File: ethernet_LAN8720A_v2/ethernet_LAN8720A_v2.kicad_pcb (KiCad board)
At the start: 2 copper layers, 55.2 x 65.4 mm, 47 parts, among them P1 SI-52003-F, P3 PoE, U1 LAN8720A-CP, U2 ASV-50.000MHZ-E-T

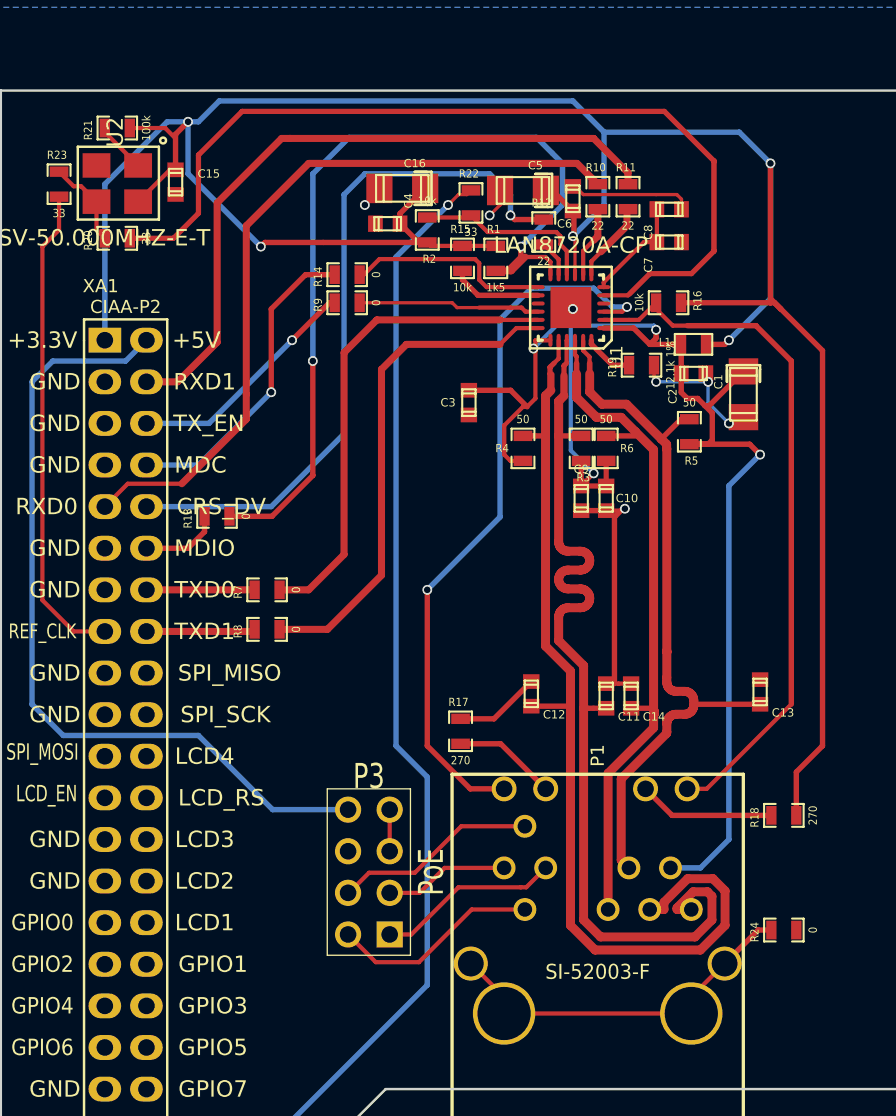
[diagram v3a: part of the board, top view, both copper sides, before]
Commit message: Acomdado de serigrafía y algunas pistas para que el pleno llegue a toda la placa.
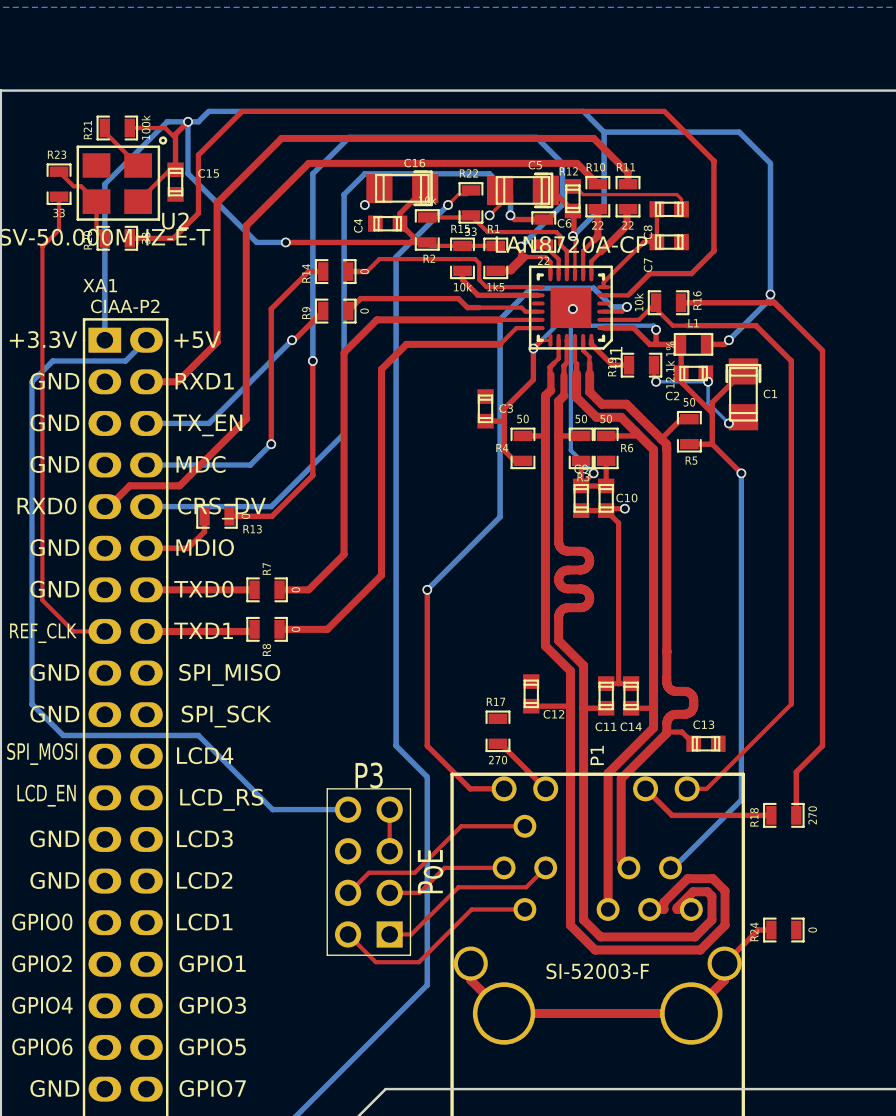
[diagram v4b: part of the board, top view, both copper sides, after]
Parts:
- moved C13 4.57 mm to (134.2, 108.6), turned to 180 degrees
- moved R17 2.29 mm to (121.5, 107.9)
- moved C3 1.09 mm to (120.8, 88.2), turned to 270 degrees
- moved R9 0.86 mm to (111.6, 82.2)
- moved R14 0.72 mm to (111.6, 79.8)
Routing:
- net +3.3V: track 171.0 -> 162.0 mm
- net Net-(C1-Pad1): track 89.0 -> 80.9 mm
- net GND: track 43.5 -> 39.9 mm
- net Net-(P1-Pad13): track 6.34 -> 4.05 mm
- net /Circuito Principal/Rx_P: track 45.1 -> 43.0 mm
- net Net-(P1-Pad16): track 22.9 -> 24.9 mm
- net /Circuito Principal/MDC: track 19.3 -> 20.5 mm
- net Net-(R9-Pad2): track 11.1 -> 12.2 mm
- net /Circuito Principal/TXEN: track 14.5 -> 13.6 mm
- net Net-(R14-Pad2): track 12.6 -> 13.2 mm
- net /Circuito Principal/Tx_P: track 59.0 -> 58.5 mm

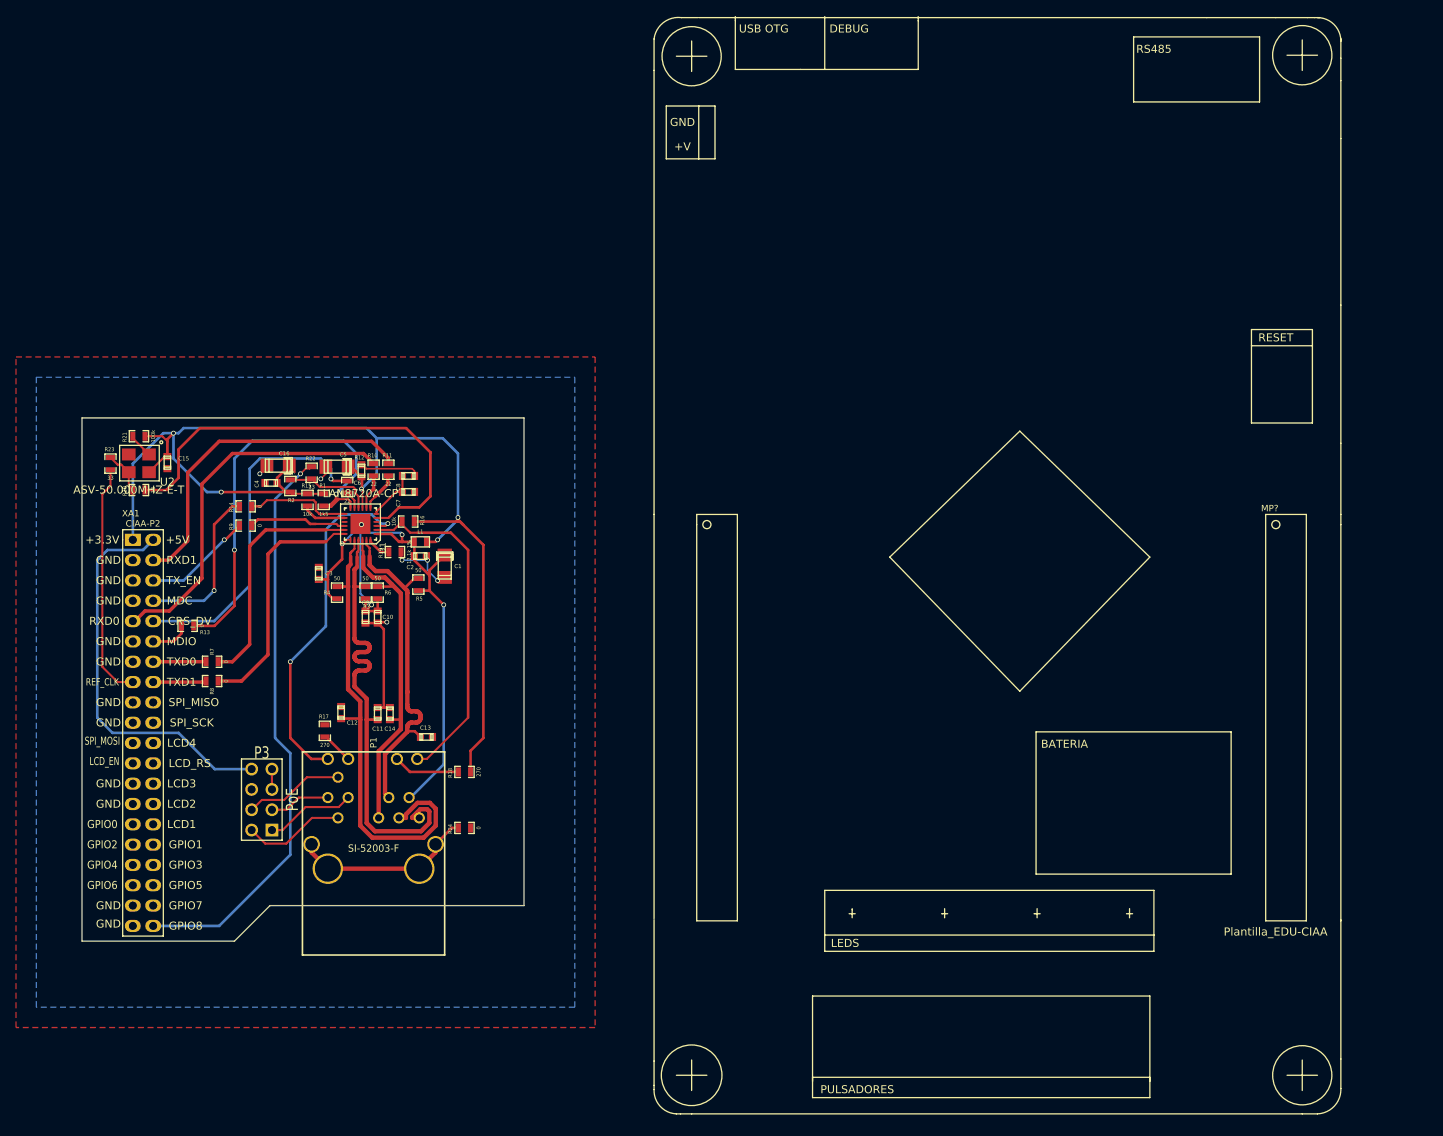
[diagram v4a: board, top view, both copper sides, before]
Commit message: Mejoro conección entre planos de tierra. Separo chasis de tierra. Vía fences.
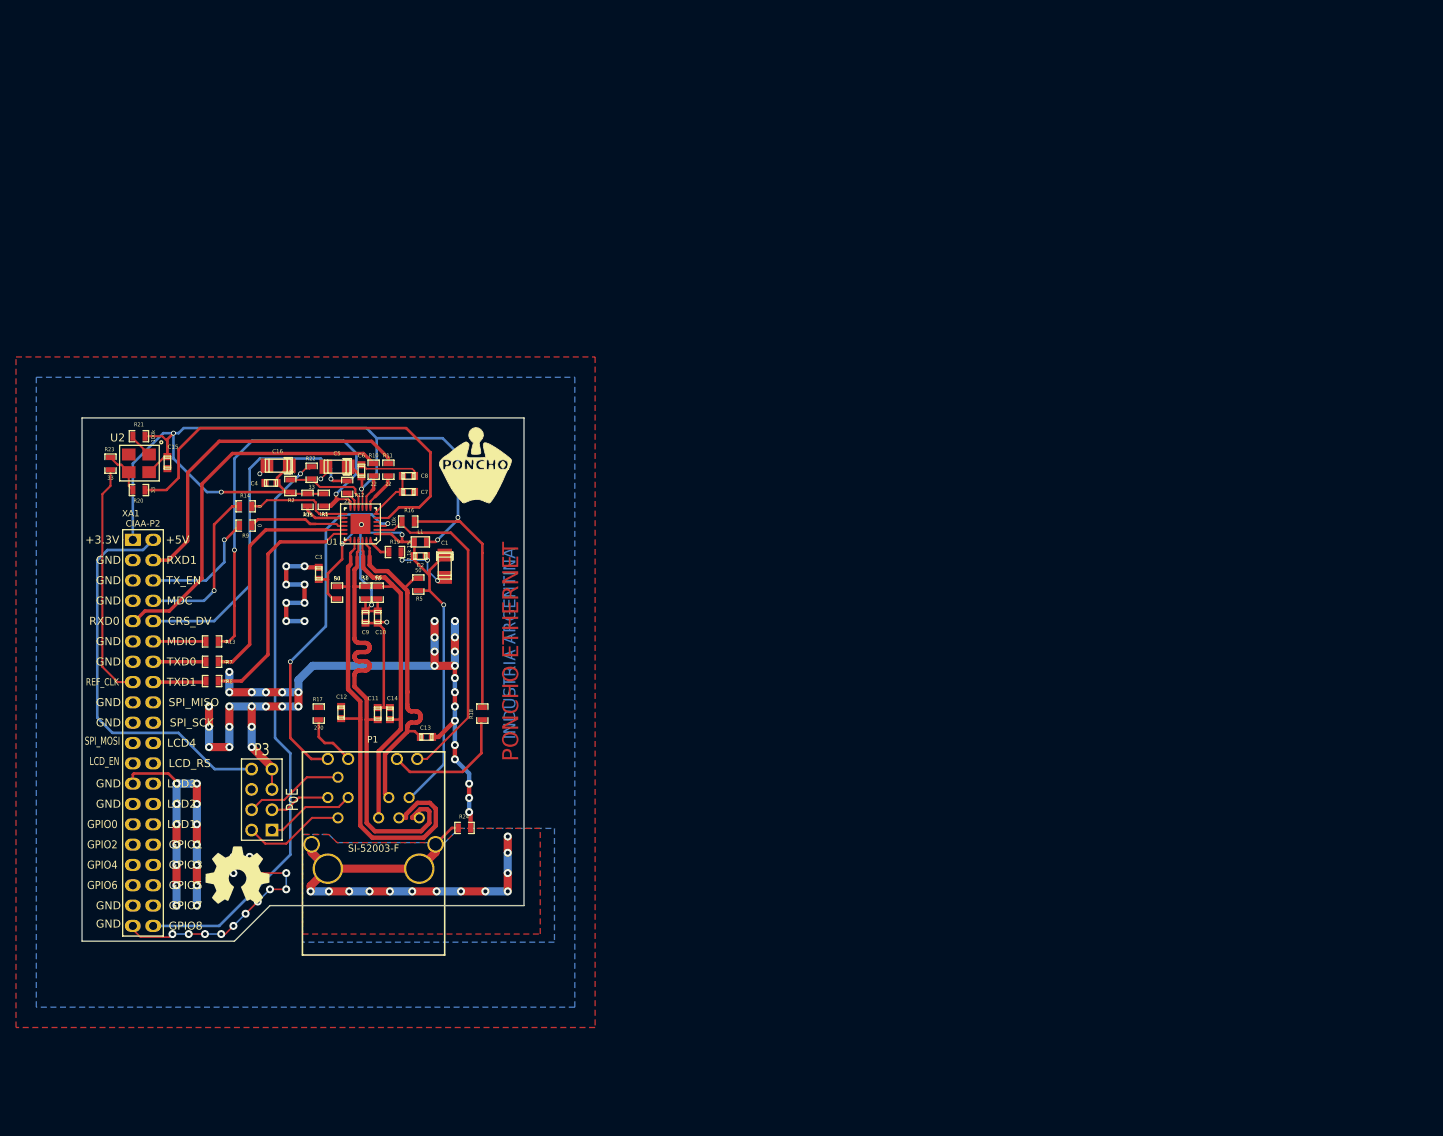
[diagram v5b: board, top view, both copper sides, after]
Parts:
- removed MP?: Plantilla_EDU-CIAA, eth:Plantilla_EDU-CIAA
- added G***: LOGO, eth:Logo_Poncho, F.Cu at (140.3, 74.7)
- added G101: Logo_OSHWA, eth:Logo_OSHWA, F.Cu at (110.6, 125.9)
- moved R18 7.63 mm to (141.2, 105.7), turned to 90 degrees
- moved R13 3.62 mm to (107.5, 96.7)
- moved R17 2.29 mm to (120.8, 105.7)
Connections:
- net Net-(P1-Pad16) renamed /Circuito Principal/CHASIS
- P3 pad 6: (no net) -> Net-(P3-Pad6)
- U1 pad 15: (no net) -> /Circuito Principal/PHY_nRESET
- U1 pad 4: (no net) -> Net-(U1-Pad4)
- XA1 pad 58: (no net) -> /Circuito Principal/MISO
- XA1 pad 60: (no net) -> /Circuito Principal/spiSCK
- XA1 pad 61: (no net) -> /Circuito Principal/MOSI
- XA1 pad 62: (no net) -> /Circuito Principal/LCD4
- XA1 pad 63: (no net) -> /Circuito Principal/LCD_EN
- XA1 pad 64: (no net) -> /Circuito Principal/RS
- XA1 pad 66: (no net) -> /Circuito Principal/LCD3
- XA1 pad 68: (no net) -> /Circuito Principal/LCD2
- XA1 pad 69: (no net) -> /Circuito Principal/GPIO0
- XA1 pad 70: (no net) -> /Circuito Principal/LCD1
- XA1 pad 71: (no net) -> /Circuito Principal/GPIO2
- XA1 pad 72: (no net) -> /Circuito Principal/GPIO1
- XA1 pad 73: (no net) -> /Circuito Principal/GPIO4
- XA1 pad 74: (no net) -> /Circuito Principal/GPIO3
- XA1 pad 75: (no net) -> /Circuito Principal/GPIO6
- XA1 pad 76: (no net) -> /Circuito Principal/GPIO5
- XA1 pad 78: (no net) -> /Circuito Principal/GPIO7
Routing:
- net GND: track 39.9 -> 234.2 mm, vias 7 -> 78
- net /Circuito Principal/CHASIS: track 24.9 -> 67.9 mm, vias 0 -> 13
- net +3.3V: track 162.0 -> 152.4 mm
- net Net-(P1-Pad14): track 8.35 -> 16.4 mm
- net Net-(P1-Pad13): track 4.05 -> 7.03 mm
- net /Circuito Principal/MDIO: track 4.91 -> 6.60 mm
- net /Circuito Principal/TXEN: track 13.6 -> 15.3 mm
- added copper zone on B.Cu, net /Circuito Principal/CHASIS
- added copper zone on F.Cu, net /Circuito Principal/CHASIS
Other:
- board text added: "INDUSTRIA ARGENTINA"
- board text added: "PONCHO ETHERNET"

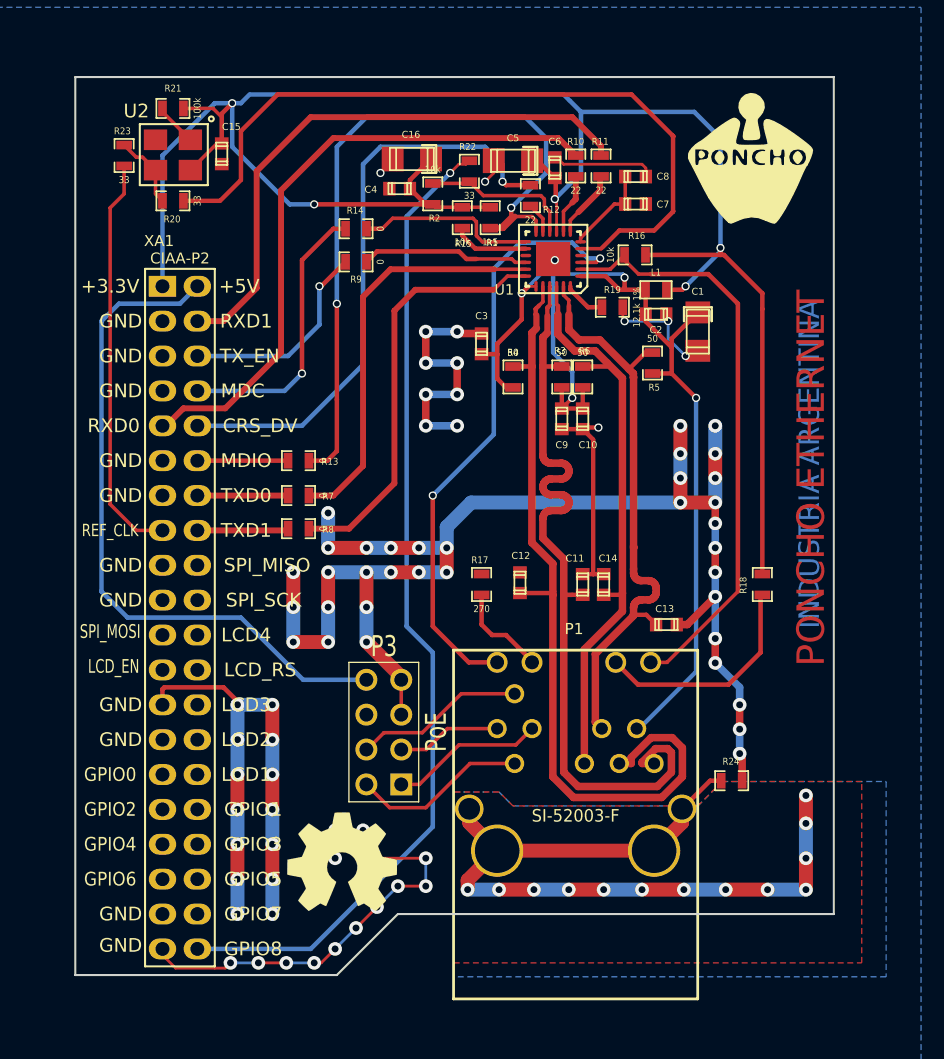
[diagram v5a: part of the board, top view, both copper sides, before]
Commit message: Agrando vías para fabricación nacional 1mm/0,5mm. Mejoro chasis vs. GND. Detalles de ruteo.
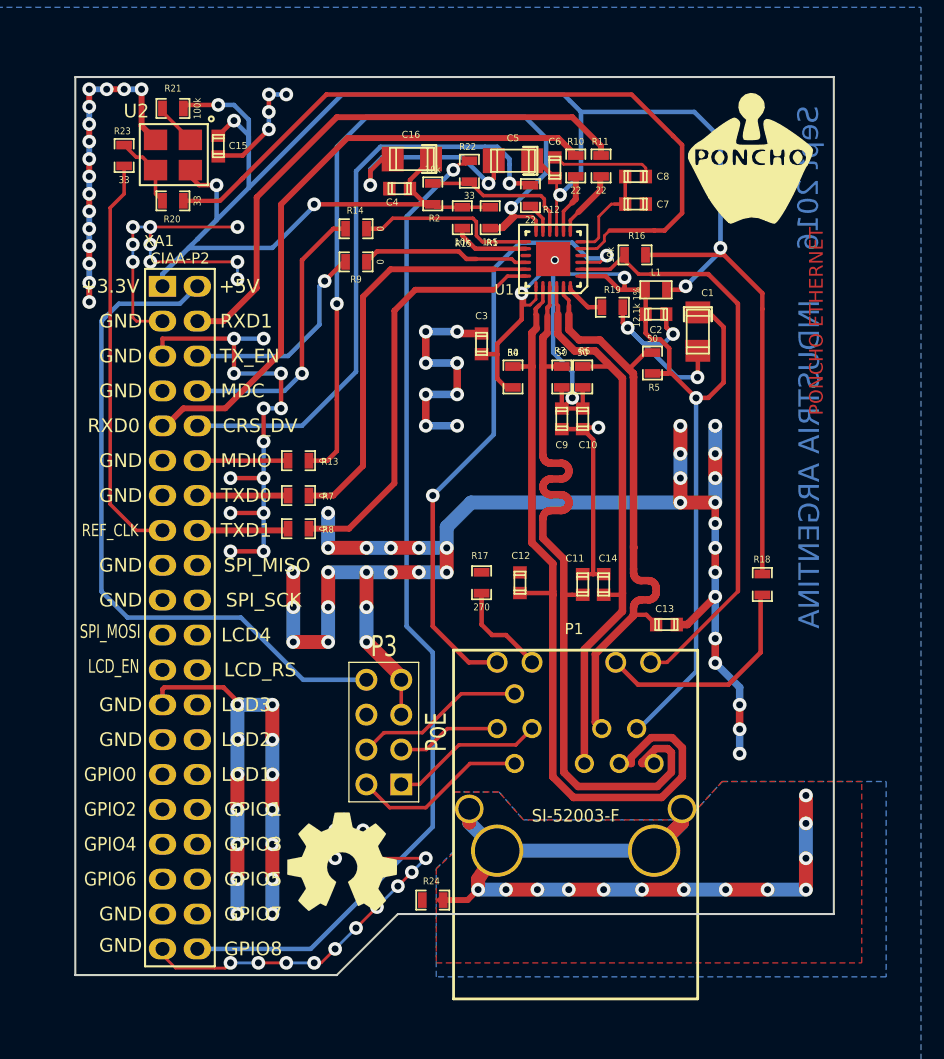
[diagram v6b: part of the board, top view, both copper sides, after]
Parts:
- moved R24 23.4 mm to (117.2, 128.7), turned to 180 degrees
- moved C15 0.61 mm to (101.6, 73.8)
- moved R17 0.13 mm to (120.8, 105.6)
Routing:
- net GND: track 234.2 -> 345.9 mm, vias 78 -> 120
- net Net-(R20-Pad2): track 103.1 -> 59.1 mm
- net Net-(C1-Pad1): track 80.9 -> 90.0 mm
- net +3.3V: track 152.4 -> 159.4 mm, vias 5 -> 7
- net /Circuito Principal/CHASIS: track 67.9 -> 61.2 mm
- net Net-(C7-Pad1): track 6.56 -> 8.10 mm
- net /Circuito Principal/LED_LINK: track 44.2 -> 45.3 mm
- net /Circuito Principal/RXD1: track 42.1 -> 41.0 mm
- net /Circuito Principal/RXD0: track 46.2 -> 45.6 mm
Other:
- board text added: "Sept 2016"
